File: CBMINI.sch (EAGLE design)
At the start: 47 parts, among them J1 USB_B_PTH, SW1 SWITCH-DPDT3, U1 MCP2551, X1 INPUT, X2 OUTPUT

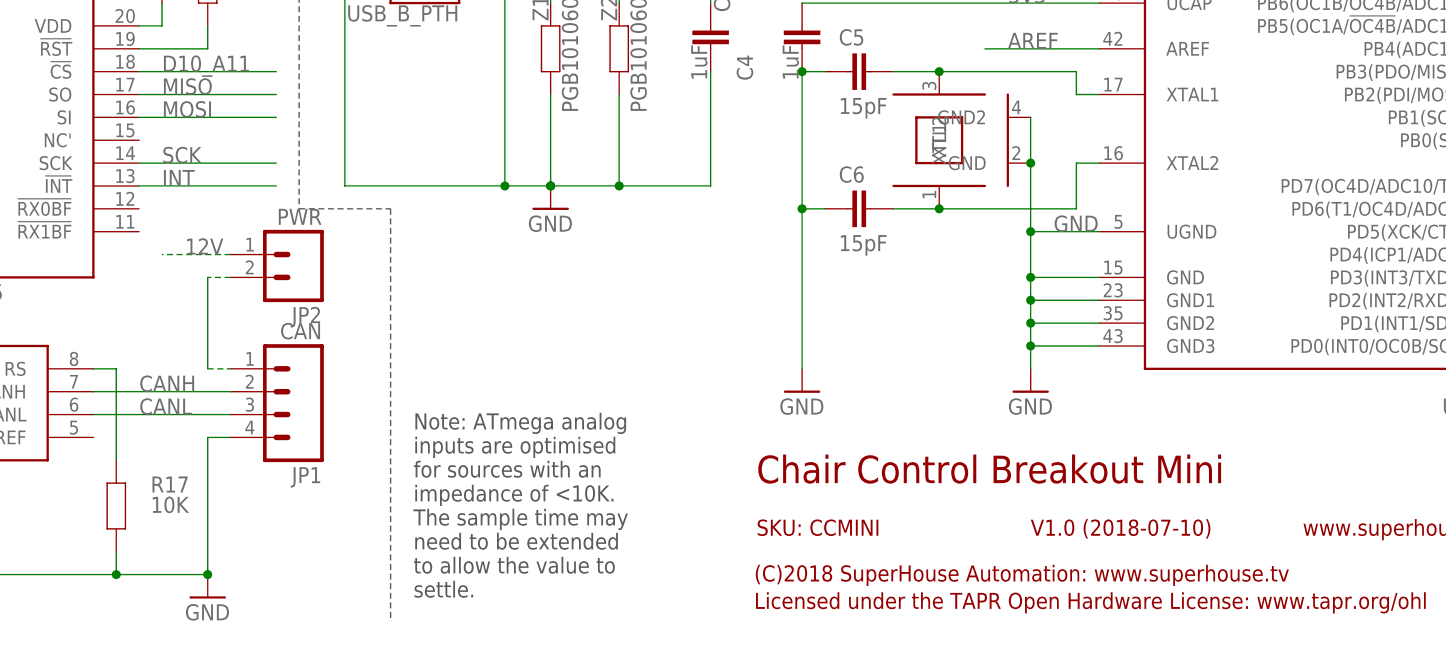
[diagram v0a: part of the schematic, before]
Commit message: Added CAN bus interrupt connection to D2 for v1.1 release
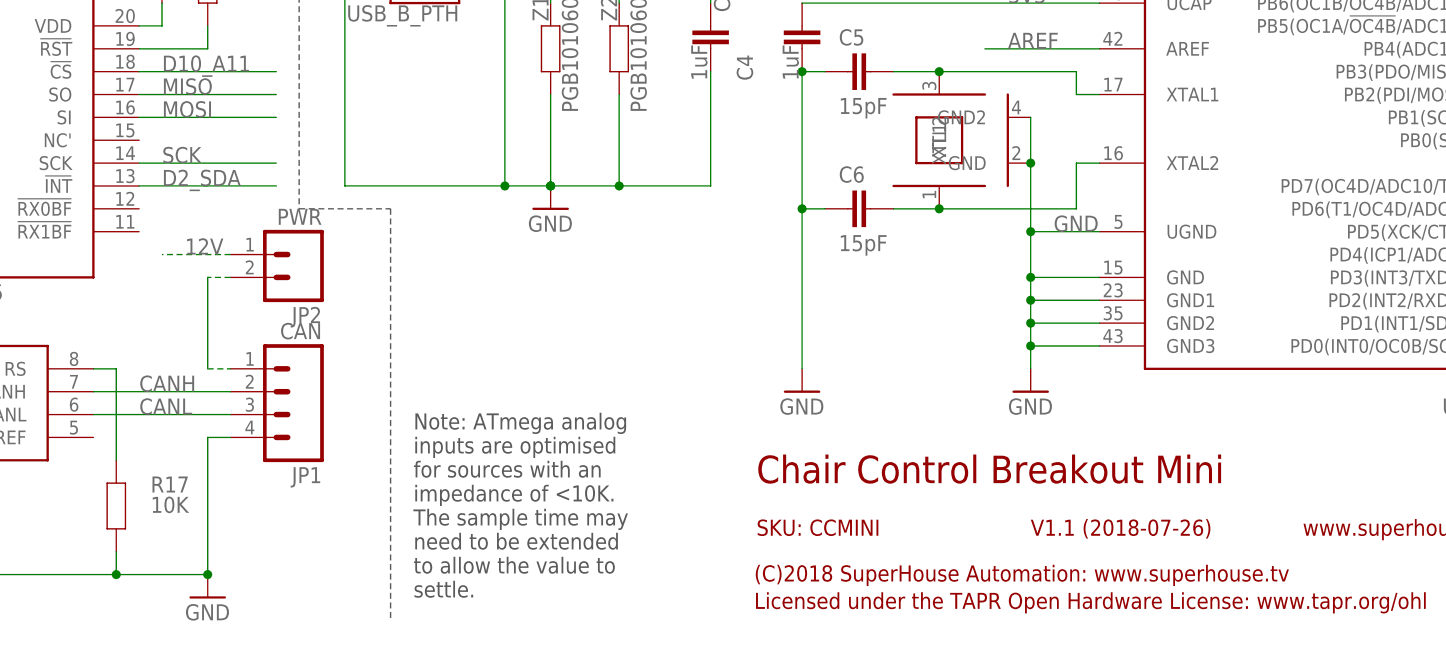
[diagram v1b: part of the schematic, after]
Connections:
- removed net INT: U$4.!INT
- net D2_SDA: now also U$4.!INT
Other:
- note added: "V1.1 (2018-07-26)"
- note removed: "V1.0 (2018-07-10)"
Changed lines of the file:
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@@
 <text x="185.42" y="119.38" size="2.54" layer="94" ratio="12">ATmega32u4 MCU</text>
 <text x="142.24" y="20.32" size="3.048" layer="94">Chair Control Breakout Mini</text>
-<text x="172.72" y="14.478" size="1.778" layer="94">V1.0 (2018-07-10)</text>
+<text x="172.72" y="14.478" size="1.778" layer="94">V1.1 (2018-07-26)</text>
 <text x="142.24" y="14.478" size="1.778" layer="94">SKU: CCMINI</text>
 <text x="141.986" y="9.398" size="1.778" layer="94">(C)2018 SuperHouse Automation: www.superhouse.tv</text>
@@
 <pinref part="U$11" gate="G$1" pin="PD1(INT1/SDA)"/>
 </segment>
+<segment>
+<pinref part="U$4" gate="G$1" pin="!INT"/>
+<wire x1="73.66" y1="53.34" x2="88.9" y2="53.34" width="0.1524" layer="91"/>
+<label x="76.2" y="53.34" size="1.778" layer="95"/>
+</segment>
 </net>
 <net name="D3_SCL" class="0">
@@
 </segment>
 </net>
-<net name="INT" class="0">
-<segment>
-<pinref part="U$4" gate="G$1" pin="!INT"/>
-<wire x1="73.66" y1="53.34" x2="88.9" y2="53.34" width="0.1524" layer="91"/>
-<label x="76.2" y="53.34" size="1.778" layer="95"/>
-</segment>
-</net>
